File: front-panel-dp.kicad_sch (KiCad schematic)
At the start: 31 parts, among them J2501 DisplayPort-Mini_Pulse_E9320-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, T2501 Choke_DLW21SN900HQ2L, T2502 Choke_DLW21SN900HQ2L, T2505 Choke_DLW21SN900HQ2L, U2501 TPD4E05U06QDQARQ1, U2503 SN65MLVD200A, U2504 TPD4E05U06QDQARQ1

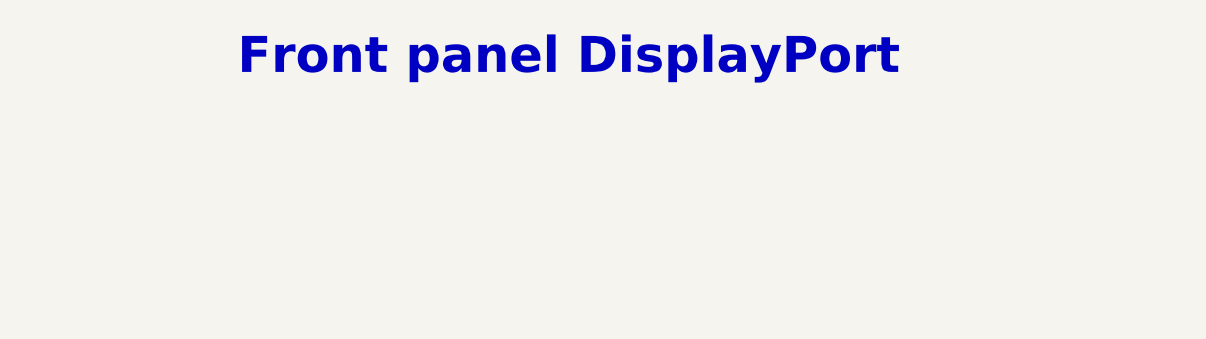
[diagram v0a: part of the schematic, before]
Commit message: [#100282] Add missing schematic sheet names and align them all
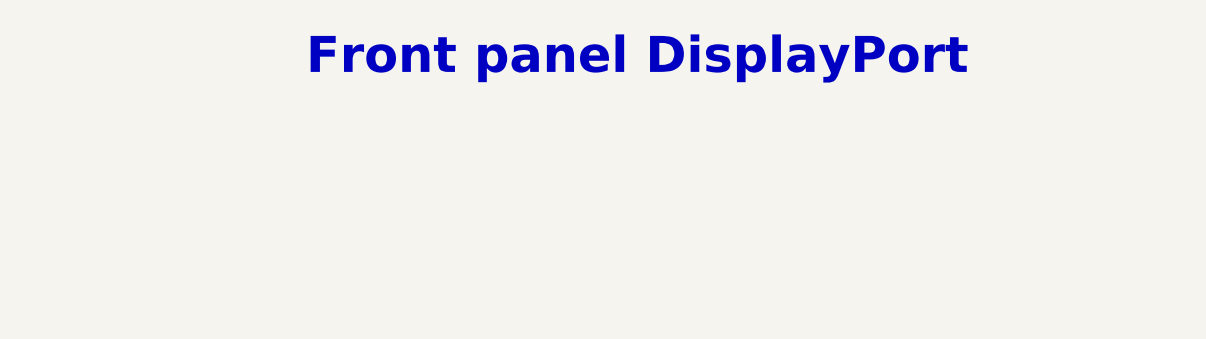
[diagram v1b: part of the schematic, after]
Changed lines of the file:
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@@
 	(text "Front panel DisplayPort"
 		(exclude_from_sim no)
-		(at 203.2 38.1 0)
+		(at 210.82 38.1 0)
 		(effects
 			(font

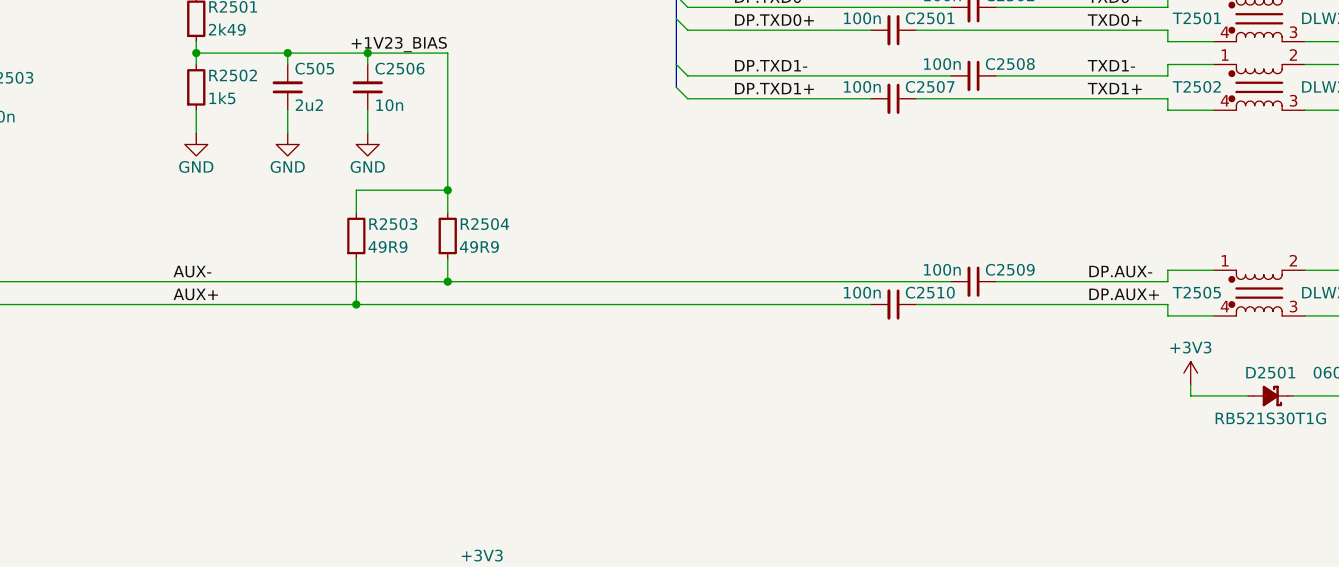
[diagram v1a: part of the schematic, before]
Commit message: [#100501] Fix DP.AUX +/- mixup
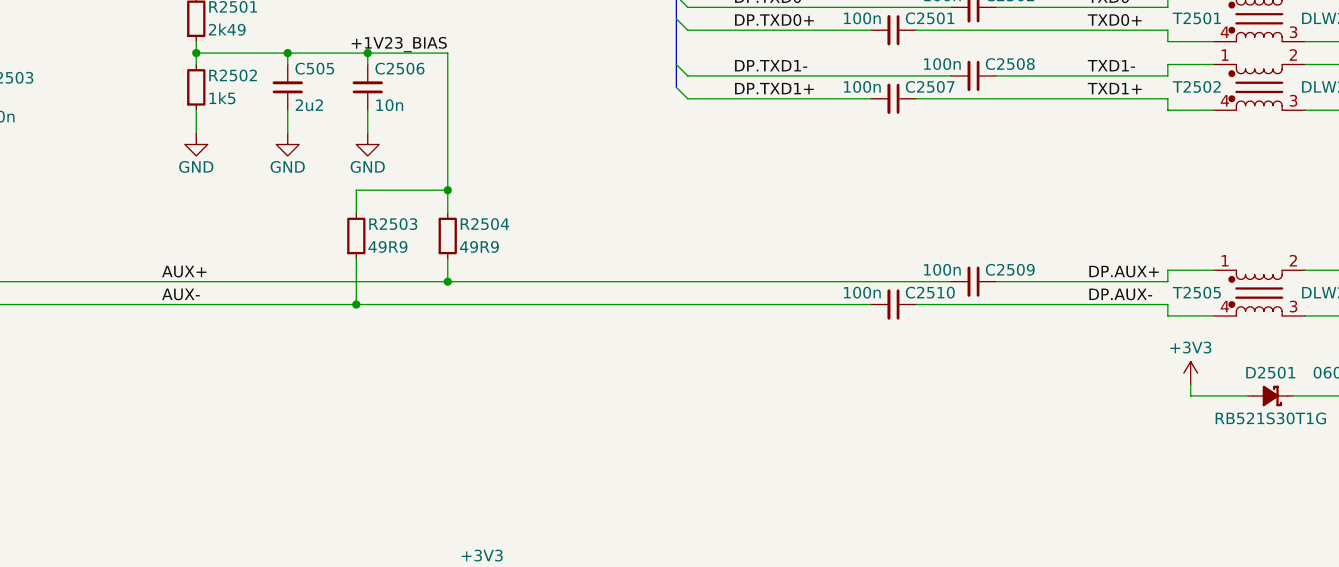
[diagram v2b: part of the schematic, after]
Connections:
- net AUX+: now also C2509.2, R2504.1, U2503.6 (A); no longer C2510.2, R2503.1, U2503.7 (B)
- net AUX-: now also C2510.2, R2503.1, U2503.7 (B); no longer C2509.2, R2504.1, U2503.6 (A)
- net DP.AUX+: now also C2509.1, T2505.1; no longer C2510.1, T2505.4
- net DP.AUX-: now also C2510.1, T2505.4; no longer C2509.1, T2505.1
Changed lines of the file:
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@@
+		)
+	)
+	(label "DP.AUX-"
+		(at 217.17 128.27 0)
+		(effects
+			(font
+				(size 1.27 1.27)
+			)
+			(justify left bottom)
 		)
 	)
@@
 		)
 	)
-	(label "AUX+"
-		(at 115.57 128.27 0)
-		(effects
-			(font
-				(size 1.27 1.27)
-			)
-			(justify left bottom)
-		)
-	)
 	(label "DP.TXD0+"
 		(at 177.8 97.79 0)
@@
 		)
 	)
+	(label "AUX+"
+		(at 114.3 125.73 0)
+		(effects
+			(font
+				(size 1.27 1.27)
+			)
+			(justify left bottom)
+		)
+	)
 	(label "DPCONN_AUX+"
 		(at 262.89 125.73 0)
@@
 		)
 	)
-	(label "DP.AUX+"
-		(at 217.17 128.27 0)
-		(effects
-			(font
-				(size 1.27 1.27)
-			)
-			(justify left bottom)
-		)
-	)
 	(label "DPCONN_AUX+"
 		(at 326.39 139.7 0)
@@
 		)
 	)
-	(label "DP.AUX-"
-		(at 217.17 125.73 0)
-		(effects
-			(font
-				(size 1.27 1.27)
-			)
-			(justify left bottom)
-		)
-	)
 	(label "TXD0-"
 		(at 217.17 95.25 0)
@@
 		)
 	)
+	(label "DP.AUX+"
+		(at 217.17 125.73 0)
+		(effects
+			(font
+				(size 1.27 1.27)
+			)
+			(justify left bottom)
+		)
+	)
 	(label "TXD1-"
 		(at 217.17 102.87 0)
@@
 		)
 	)
+	(label "AUX-"
+		(at 114.3 128.27 0)
+		(effects
+			(font
+				(size 1.27 1.27)
+			)
+			(justify left bottom)
+		)
+	)
 	(label "DPCONN_TXD0+"
 		(at 262.89 95.25 0)
@@
 		(effects
 			(font
-				(size 1.27 1.27)
-			)
-			(justify left bottom)
-		)
-	)
-	(label "AUX-"
-		(at 115.57 125.73 0)
-		(effects
-			(font

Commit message: [#100501] Improve front panel DP TXD lanes readability
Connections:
- net DP.TXD0+: now also C2502.2; no longer C2501.2
- net DP.TXD0-: now also C2501.2; no longer C2502.2
- net DP.TXD1+: now also C2508.2; no longer C2507.2
- net DP.TXD1-: now also C2507.2; no longer C2508.2
- net TXD0+: now also C2502.1; no longer C2501.1
- net TXD0-: now also C2501.1; no longer C2502.1
- net TXD1+: now also C2508.1; no longer C2507.1
- net TXD1-: now also C2507.1; no longer C2508.1

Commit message: [#100501] Reannotate schematic
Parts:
- renumbered C2502 to C244, C2501 to C245, C2508 to C246, C2507 to C247, C505 to C248, C2506 to C249, C2504 to C250, C2503 to C251, C2509 to C252, C2510 to C253, C2505 to C254, C2515 to C255, C2517 to C256, D2501 to D15, F2501 to F2, J2501 to J12, R2501 to R311, R2502 to R312, R2503 to R313, R2504 to R314, R2505 to R315, R2506 to R316, R2507 to R317, R2508 to R318, R2509 to R319, T2501 to T4, T2502 to T5, T2505 to T6, U2501 to U44, U2503 to U45, U2504 to U46

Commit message: [#100501] Reannotate schematic
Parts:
- renumbered C244 to C236, C245 to C237, C246 to C238, C247 to C239, C248 to C240, C249 to C241, C250 to C242, C251 to C243, C252 to C244, C253 to C245, C254 to C246, C255 to C247, C256 to C248, D15 to D26, J12 to J14, R311 to R343, R312 to R344, R313 to R345, R314 to R346, R315 to R347, R316 to R348, R317 to R349, R318 to R350, R319 to R351, T4 to T1, T5 to T2, T6 to T3, U44 to U43, U45 to U44, U46 to U45
